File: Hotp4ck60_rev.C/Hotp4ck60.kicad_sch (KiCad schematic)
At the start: 42 parts, among them J1 Conn_01x04, J2 Conn_01x02_MountingPin, U1 MAX17048, U2 BQ24075, U3 nRF52840_E73-2G4M08S1C, Y1 32.768 KHz

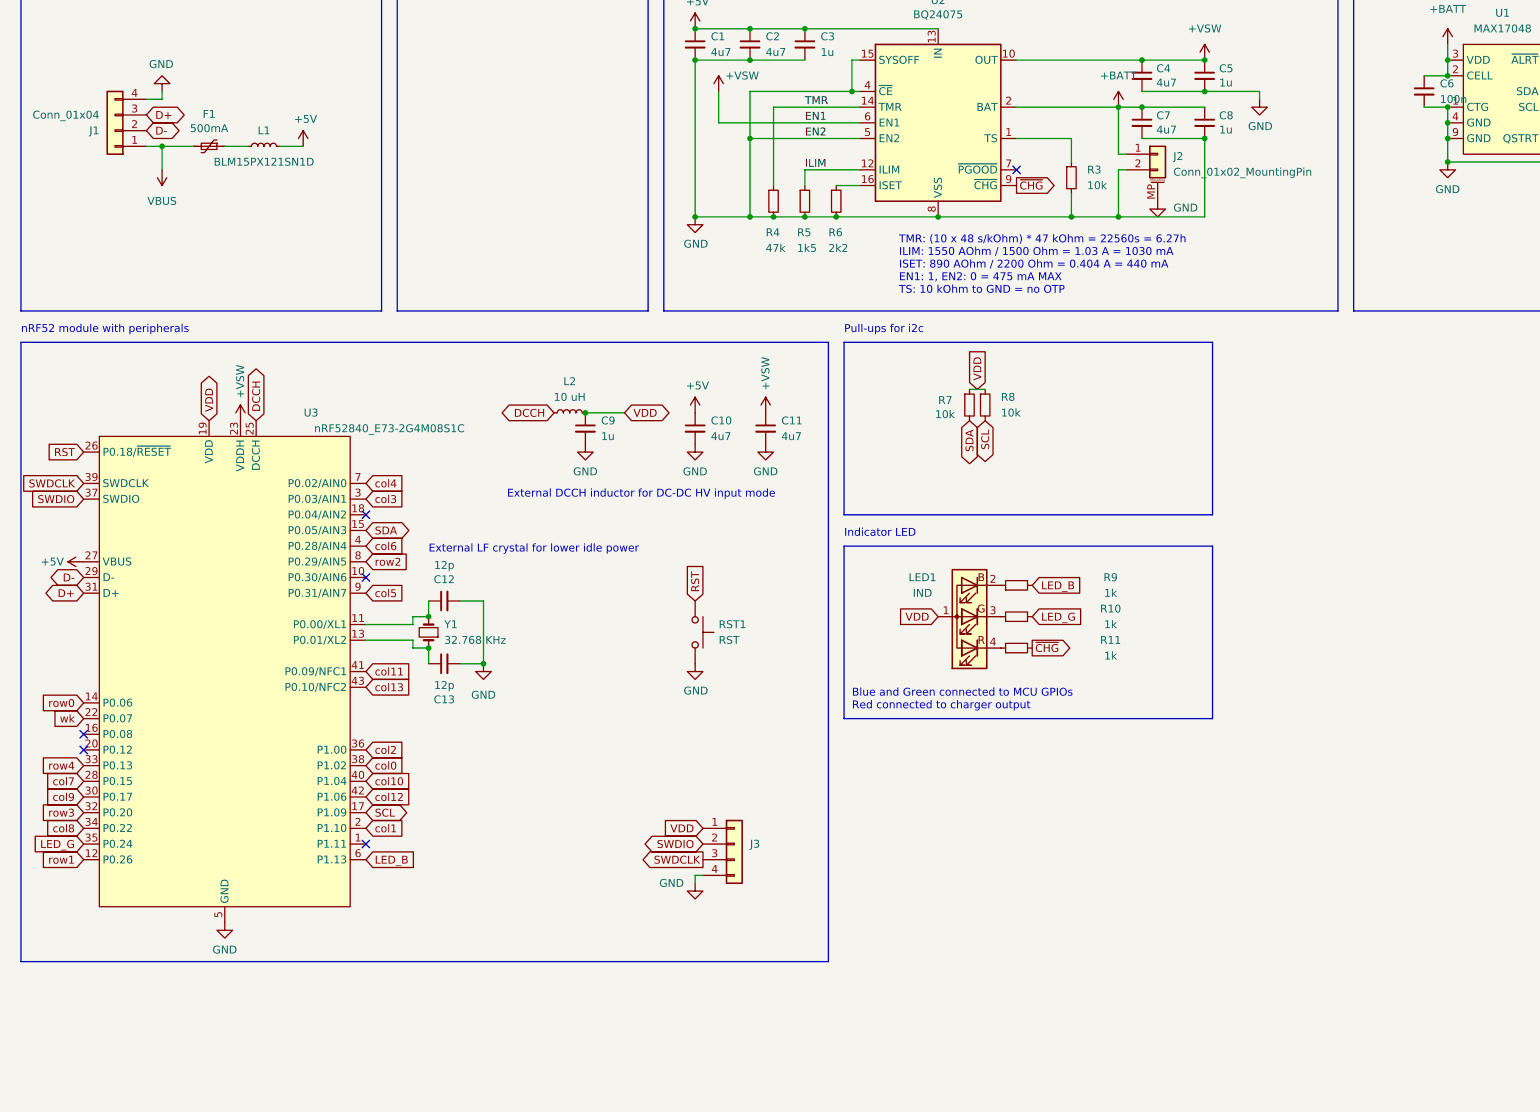
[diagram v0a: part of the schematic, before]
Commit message: rev.c 핀, 트레이스 수정
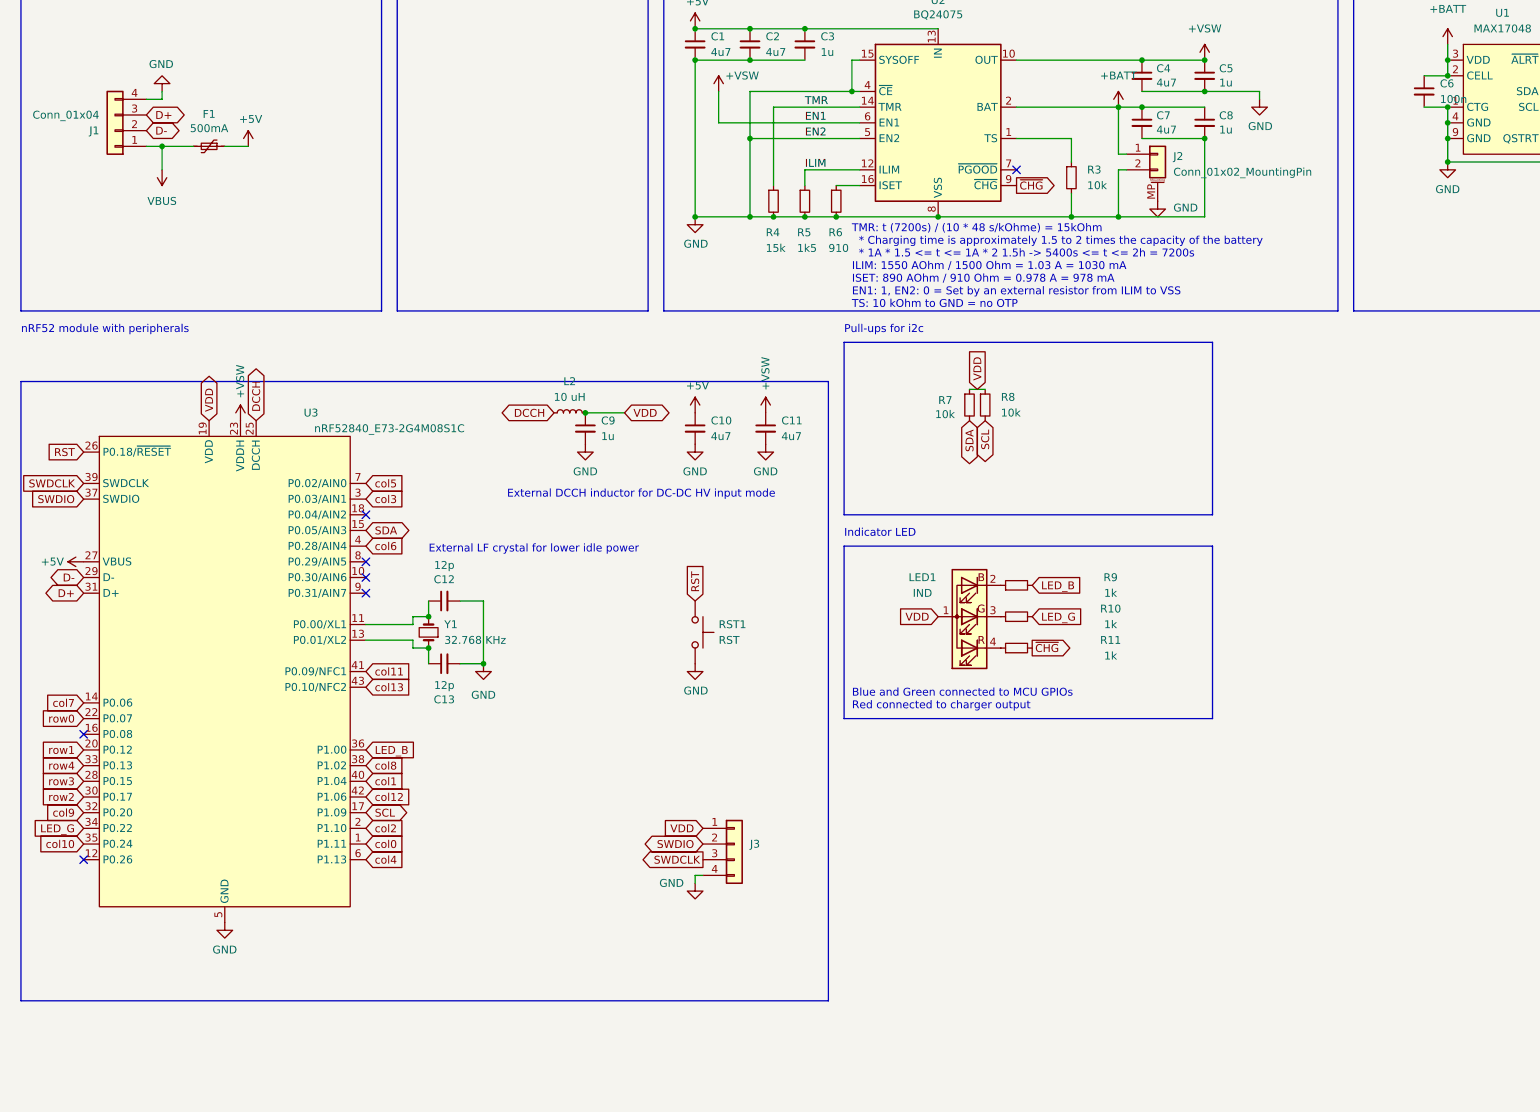
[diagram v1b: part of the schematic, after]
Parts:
- removed L1: BLM15PX121SN1D, Inductor_SMD:L_0402_1005Metric, symbol Device:L_Small
- R4: value 47k -> 15k
- R6: value 2k2 -> 910; LCSC C25879 -> C44933
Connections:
- net wk is gone; now on net row0: U3.22 (P0.07)
- net +5V: now also F1.1
- net LED_B: now also U3.36 (P1.00); no longer U3.6 (P1.13)
- net LED_G: now also U3.34 (P0.22); no longer U3.35 (P0.24)
- net col0: now also U3.1 (P1.11); no longer U3.38 (P1.02)
- net col1: now also U3.40 (P1.04); no longer U3.2 (P1.10)
- net col10: now also U3.35 (P0.24); no longer U3.40 (P1.04)
- net col2: now also U3.2 (P1.10); no longer U3.36 (P1.00)
- net col4: now also U3.6 (P1.13); no longer U3.7 (P0.02/AIN0)
- net col5: now also U3.7 (P0.02/AIN0); no longer U3.9 (P0.31/AIN7)
- net col7: now also U3.14 (P0.06); no longer U3.28 (P0.15)
- net col8: now also U3.38 (P1.02); no longer U3.34 (P0.22)
- net col9: now also U3.32 (P0.20); no longer U3.30 (P0.17)
- net row0: no longer U3.14 (P0.06)
- net row1: now also U3.20 (P0.12); no longer U3.12 (P0.26)
- net row2: now also U3.30 (P0.17); no longer U3.8 (P0.29/AIN5)
- net row3: now also U3.28 (P0.15); no longer U3.32 (P0.20)
- no-connect marks 6 -> 7
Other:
- note added: "TMR: t (7200s) / (10 * 48 s/kOhme) = 15kOhm * Charging time is approximately 1.5 to 2 times the capacity of the battery * 1A * 1.5 <= t <= 1A * 2 1.5h -> 5400s <= t <= 2h = 7200s ILIM: 1550 AOhm / 1500 Ohm = 1.03 A = 1030 mA ISET: 890 AOhm / 910 Ohm = 0.978 A = 978 mA EN1: 1, EN2: 0 = Set by an external resistor from ILIM to VSS TS: 10 kOhm to GND = no OTP"
- note removed: "TMR: (10 x 48 s/kOhm) * 47 kOhm = 22560s = 6.27h ILIM: 1550 AOhm / 1500 Ohm = 1.03 A = 1030 mA ISET: 890 AOhm / 2200 Ohm = 0.404 A = 440 mA EN1: 1, EN2: 0 = 475 mA MAX TS: 10 kOhm to GND = no OTP"

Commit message: LED 핀 수정
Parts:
- removed J1: Conn_01x04, Connector_JST:JST_SH_SM04B-SRSS-TB_1x04-1MP_P1.00mm_Horizontal, symbol Connector_Generic:Conn_01x04
- removed LED1: IND, PCM_marbastlib-various:LED_1206R, symbol PCM_marbastlib-various:LED_MHT151RGBCT
- added J1: Conn_01x04_MountingPin, Connector_JST:JST_SH_SM04B-SRSS-TB_1x04-1MP_P1.00mm_Horizontal, symbol Connector_Generic_MountingPin:Conn_01x04_MountingPin
- added LED1: LED_RAGB, symbol Device:LED_RAGB
- RST1: footprint PCM_marbastlib-various:SW_T1A2QR -> Button_Switch_SMD:SW_Push_1P1T_XKB_TS-1187A; LCSC C100056 -> C318884
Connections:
- net D+: now also J1.3 (Pin_3)
- net D-: now also J1.2 (Pin_2)
- net GND: now also J1.4 (Pin_4), J1.MP (MountPin)
- net LED_B: now also U3.34 (P0.22); no longer U3.36 (P1.00)
- net LED_G: now also U3.36 (P1.00); no longer U3.34 (P0.22)
- net VBUS: now also J1.1 (Pin_1)
- net VDD: now also LED1.2 (A)
- net at R10.1: now also LED1.3 (GK)
- net at R9.1: now also LED1.4 (BK)
- net at R11.1: now also LED1.1 (RK)
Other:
- moved on the sheet: F1, H?

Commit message: rev.C neocore
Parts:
- removed H?: MountingHole, amtra5_outline:Hotp4ckOutline, symbol Mechanical:MountingHole
- removed J1: Conn_01x04_MountingPin, Connector_JST:JST_SH_SM04B-SRSS-TB_1x04-1MP_P1.00mm_Horizontal, symbol Connector_Generic_MountingPin:Conn_01x04_MountingPin
- removed J2: Conn_01x02_MountingPin, Connector_Molex:Molex_PicoBlade_53261-0271_1x02-1MP_P1.25mm_Horizontal, symbol Connector_Generic_MountingPin:Conn_01x02_MountingPin
- removed J3: ~, Connector_PinSocket_2.54mm:PinSocket_1x04_P2.54mm_Vertical, symbol Connector_Generic:Conn_01x04
- removed LED1: LED_RAGB, symbol Device:LED_RAGB
- removed RST1: RST, Button_Switch_SMD:SW_Push_1P1T_XKB_TS-1187A, symbol Switch:SW_Push
- added H8: Mounting_Keyboard_Stabilizer:6.25u, hotp4ck:Neo60, symbol Mechanical:MountingHole
- added J1: Conn_01x05_Pin, Connector_PinHeader_2.54mm:PinHeader_1x05_P2.54mm_Vertical, symbol Connector:Conn_01x05_Pin
- added J2: Conn_01x05_Socket, Connector_PinSocket_2.54mm:PinSocket_1x05_P2.54mm_Vertical, symbol Connector:Conn_01x05_Socket
- added J3: TC2030_SWD, PCM_marbastlib-various:CON_TC2030_outlined, symbol PCM_marbastlib-various:TC2030_SWD
- added LED1: LED_ABGR, PCM_marbastlib-various:LED_1206R, symbol Device:LED_ABGR
- added SW1: SW_DIP_x01, hotp4ck:SW_DIP_HOTP4CK, symbol Switch:SW_DIP_x01
- gave numbers to parts that had none: 7
- renumbered L2 to L1, U3 to U1, U1 to U3
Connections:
- net +BATT: now also J1.5 (Pin_5)
- net +VSW: now also SW1.2; no longer C11.1, U1.23 (VDDH)
- net D+: now also J1.3 (Pin_3)
- net D-: now also J1.2 (Pin_2)
- net GND: now also J1.4 (Pin_4), J2.4 (Pin_4), J3.5 (GND)
- net LED_B: now also U1.12 (P0.26); no longer U1.34 (P0.22)
- net LED_G: now also U1.10 (P0.30/AIN6); no longer U1.36 (P1.00)
- net RST: now also J2.5 (Pin_5), J3.3 (~{RST})
- net SWDCLK: now also J2.3 (Pin_3), J3.4 (SWCLK)
- net SWDIO: now also J2.2 (Pin_2), J3.2 (SWDIO)
- net VBUS: now also J1.1 (Pin_1)
- net VDD: now also J2.1 (Pin_1), J3.1 (VCC), LED1.1 (A)
- net col1: now also U1.2 (P1.10); no longer U1.40 (P1.04)
- net col10: now also U1.40 (P1.04); no longer U1.35 (P0.24)
- net col2: now also U1.38 (P1.02); no longer U1.2 (P1.10)
- net col8: now also U1.36 (P1.00); no longer U1.38 (P1.02)
- net col9: now also U1.34 (P0.22); no longer U1.32 (P0.20)
- net row0: now also U1.32 (P0.20); no longer U1.22 (P0.07)
- net row1: now also U1.28 (P0.15); no longer U1.20 (P0.12)
- net row2: now also U1.20 (P0.12); no longer U1.30 (P0.17)
- net row3: now also U1.22 (P0.07); no longer U1.28 (P0.15)
- net row4: now also U1.35 (P0.24); no longer U1.33 (P0.13)
- net at R10.1: now also LED1.3 (GK)
- net at R11.1: now also LED1.4 (RK)
- net at R9.1: now also LED1.2 (BK)
- new net +VDDH: C11.1, SW1.1, U1.23 (VDDH)
- no-connect marks 7 -> 8
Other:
- moved on the sheet: C10, C11, C9, F1, L1, R9

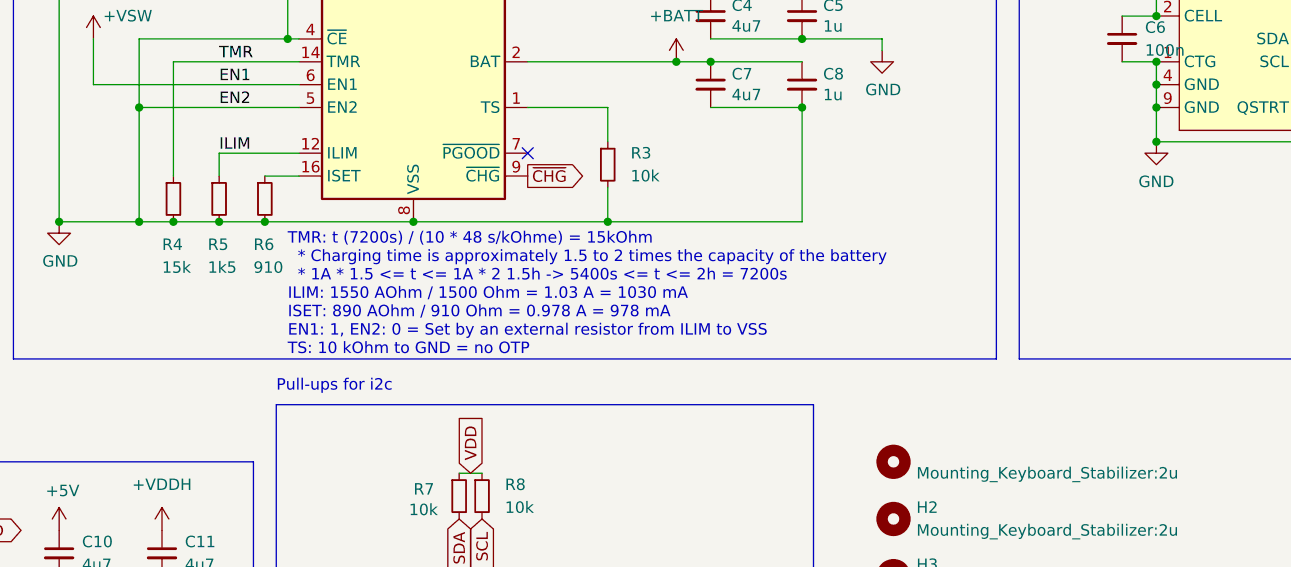
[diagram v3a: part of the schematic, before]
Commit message: 전우너 관리 IC 타이머 저항 수정
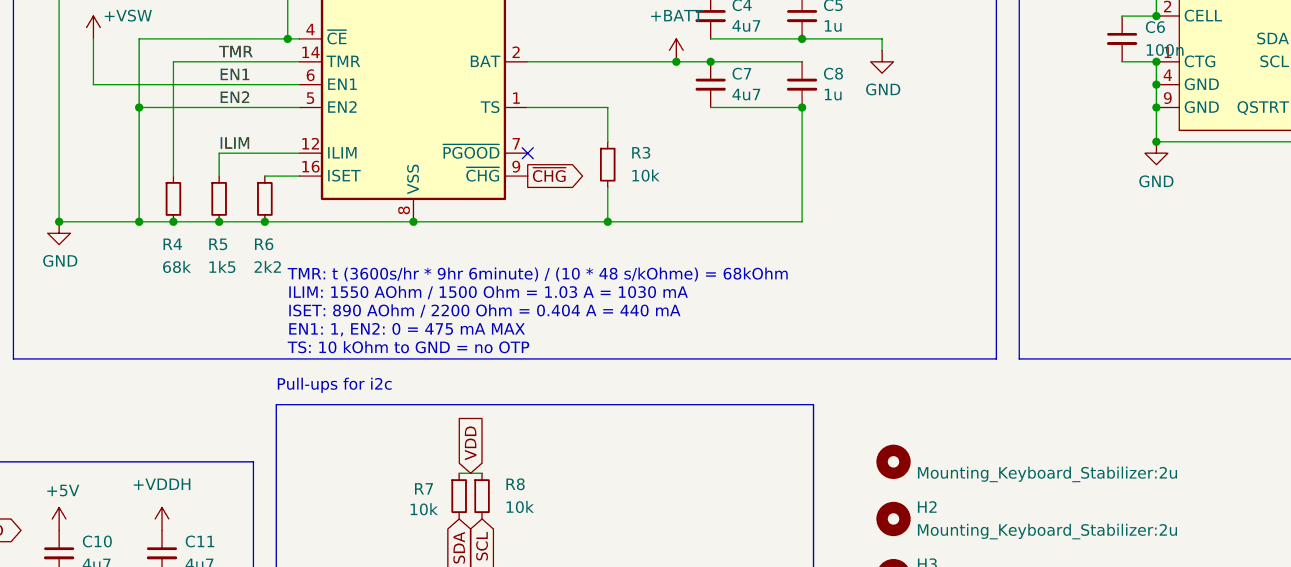
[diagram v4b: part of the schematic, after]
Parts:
- R4: value 15k -> 68k; footprint Resistor_SMD:R_0402_1005Metric -> Resistor_SMD:R_0805_2012Metric; LCSC C25792 -> C17801
- R6: value 910 -> 2k2; LCSC C44933 -> C25879
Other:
- note added: "TMR: t (3600s/hr * 9hr 6minute) / (10 * 48 s/kOhme) = 68kOhm ILIM: 1550 AOhm / 1500 Ohm = 1.03 A = 1030 mA ISET: 890 AOhm / 2200 Ohm = 0.404 A = 440 mA EN1: 1, EN2: 0 = 475 mA MAX TS: 10 kOhm to GND = no OTP"
- note removed: "TMR: t (7200s) / (10 * 48 s/kOhme) = 15kOhm * Charging time is approximately 1.5 to 2 times the capacity of the battery * 1A * 1.5 <= t <= 1A * 2 1.5h -> 5400s <= t <= 2h = 7200s ILIM: 1550 AOhm / 1500 Ohm = 1.03 A = 1030 mA ISET: 890 AOhm / 910 Ohm = 0.978 A = 978 mA EN1: 1, EN2: 0 = Set by an external resistor from ILIM to VSS TS: 10 kOhm to GND = no OTP"
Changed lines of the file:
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@@
 		)
 	)
-	(text "TMR: t (7200s) / (10 * 48 s/kOhme) = 15kOhm\n  * Charging time is approximately 1.5 to 2 times the capacity of the battery\n  * 1A * 1.5 <= t <= 1A * 2 1.5h -> 5400s <= t <= 2h = 7200s\nILIM: 1550 AOhm / 1500 Ohm = 1.03 A = 1030 mA\nISET: 890 AOhm / 910 Ohm = 0.978 A = 978 mA\nEN1: 1, EN2: 0 = Set by an external resistor from ILIM to VSS\nTS: 10 kOhm to GND = no OTP"
+	(text "TMR: t (3600s/hr * 9hr 6minute) / (10 * 48 s/kOhme) = 68kOhm\nILIM: 1550 AOhm / 1500 Ohm = 1.03 A = 1030 mA\nISET: 890 AOhm / 2200 Ohm = 0.404 A = 440 mA\nEN1: 1, EN2: 0 = 475 mA MAX\nTS: 10 kOhm to GND = no OTP"
 		(exclude_from_sim no)
 		(at 158.75 79.756 0)
@@
 			)
 		)
-		(property "Value" "910"
+		(property "Value" "2k2"
 			(at 154.94 69.85 0)
 			(effects
@@
 			)
 		)
-		(property "LCSC" "C44933"
+		(property "LCSC" "C25879"
 			(at 156.21 62.23 0)
 			(effects
@@
 			)
 		)
-		(property "Value" "15k"
+		(property "Value" "68k"
 			(at 144.78 69.85 0)
 			(effects
@@
 			)
 		)
-		(property "Footprint" "Resistor_SMD:R_0402_1005Metric"
+		(property "Footprint" "Resistor_SMD:R_0805_2012Metric"
 			(at 146.05 62.23 0)
 			(effects
@@
 			)
 		)
-		(property "LCSC" "C25792"
+		(property "LCSC" "C17801"
 			(at 146.05 62.23 0)
 			(effects
